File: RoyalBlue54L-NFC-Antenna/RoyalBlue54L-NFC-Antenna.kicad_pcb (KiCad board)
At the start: 2 copper layers, 23 x 58 mm, 2 parts, among them J1 Conn_01x02

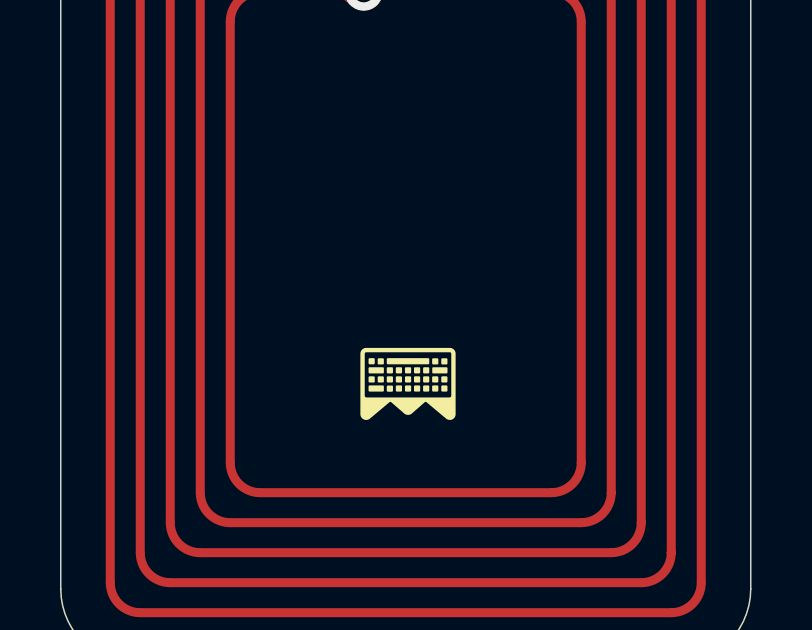
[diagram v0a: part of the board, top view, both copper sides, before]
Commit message: Added PCBWay logo
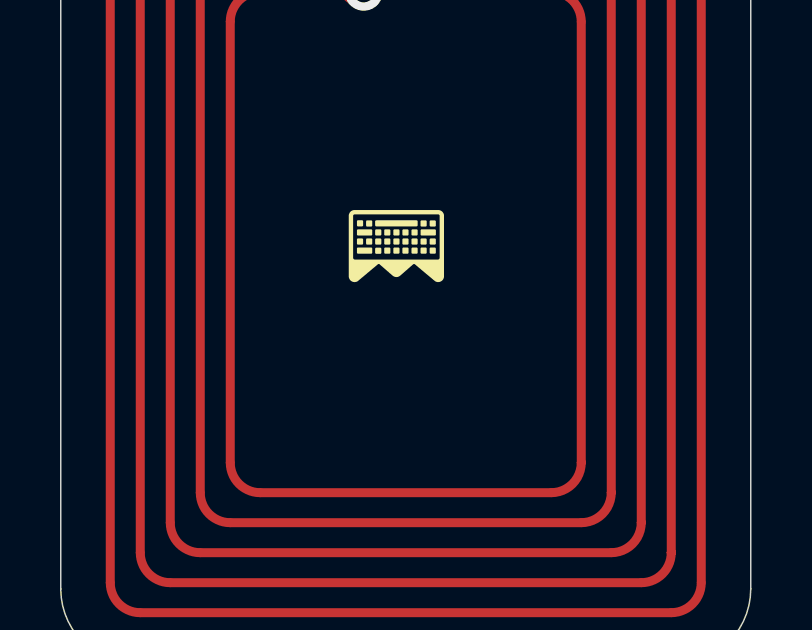
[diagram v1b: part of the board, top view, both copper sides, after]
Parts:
- moved REF** 4.61 mm to (152.7, 114.4)
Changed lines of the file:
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@@
 	(footprint "LordsBoards-Symbol:LordsBoardsLogo_Small_Silk"
 		(layer "F.Cu")
-		(at 153.1125 118.976103 180)
+		(at 152.725 114.38 180)
 		(property "Reference" "REF**"
 			(at 0 -0.5 180)
